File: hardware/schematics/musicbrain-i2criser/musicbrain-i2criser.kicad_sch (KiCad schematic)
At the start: 2 parts, among them J1 BUS, J2 NAAR FRONT

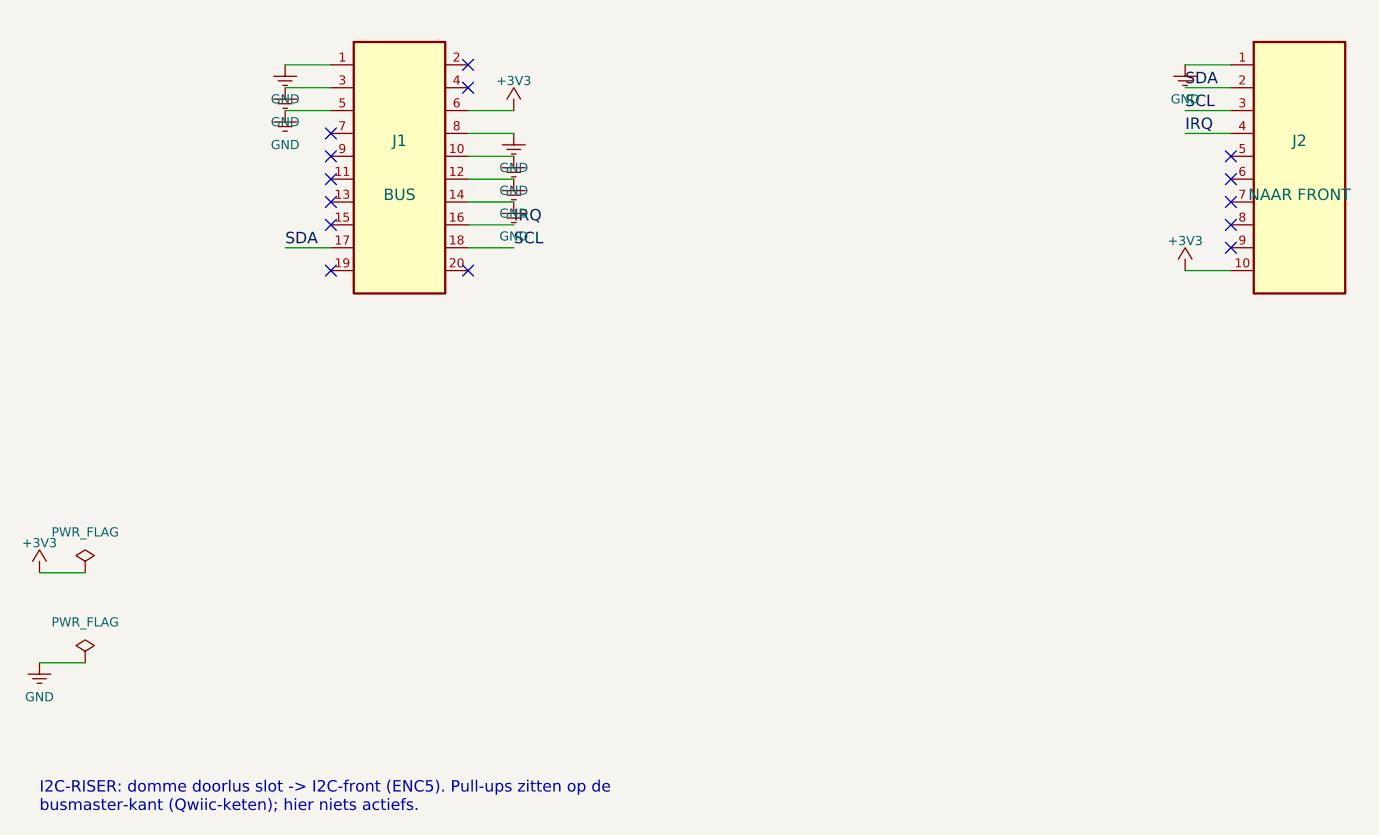
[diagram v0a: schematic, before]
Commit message: Gen 2 stap 2+3a: bus.py + i2criser rev 2.0 (2x12, H=50) DRC 0/0
bus.py = één bron van waarheid voor bus-generatie 2 (spiegel van
spi-bus-spec v2.0): H=50, kaartbreedte 80, slotsteek 20,32, de 24-pins
SLOT-map, de 2x12-footprints en de front-standaard. Generators tikken de
pinout niet meer zelf over.

i2criser rev 2.0 = eerste bord op gen 2 (dom = snelste validatie van de
keten): 40x50 (de 2x12 spant 27,94 -> 28 mm was te smal), J1 2x12, J2 1x10
ongewijzigd. Routing-les: laan-volgorde is kritisch (SDA komt van de kolom
waar SCL naartoe moet -> SDA jogt meteen westwaarts); +3V3 gebruikt de
4 mm vrije strook zuid van J1 i.p.v. de krappe rijcorridor.
ERC 0 / netcheck OK / DRC 0/0.

Co-Authored-By: Claude Fable 5 <noreply@anthropic.com>
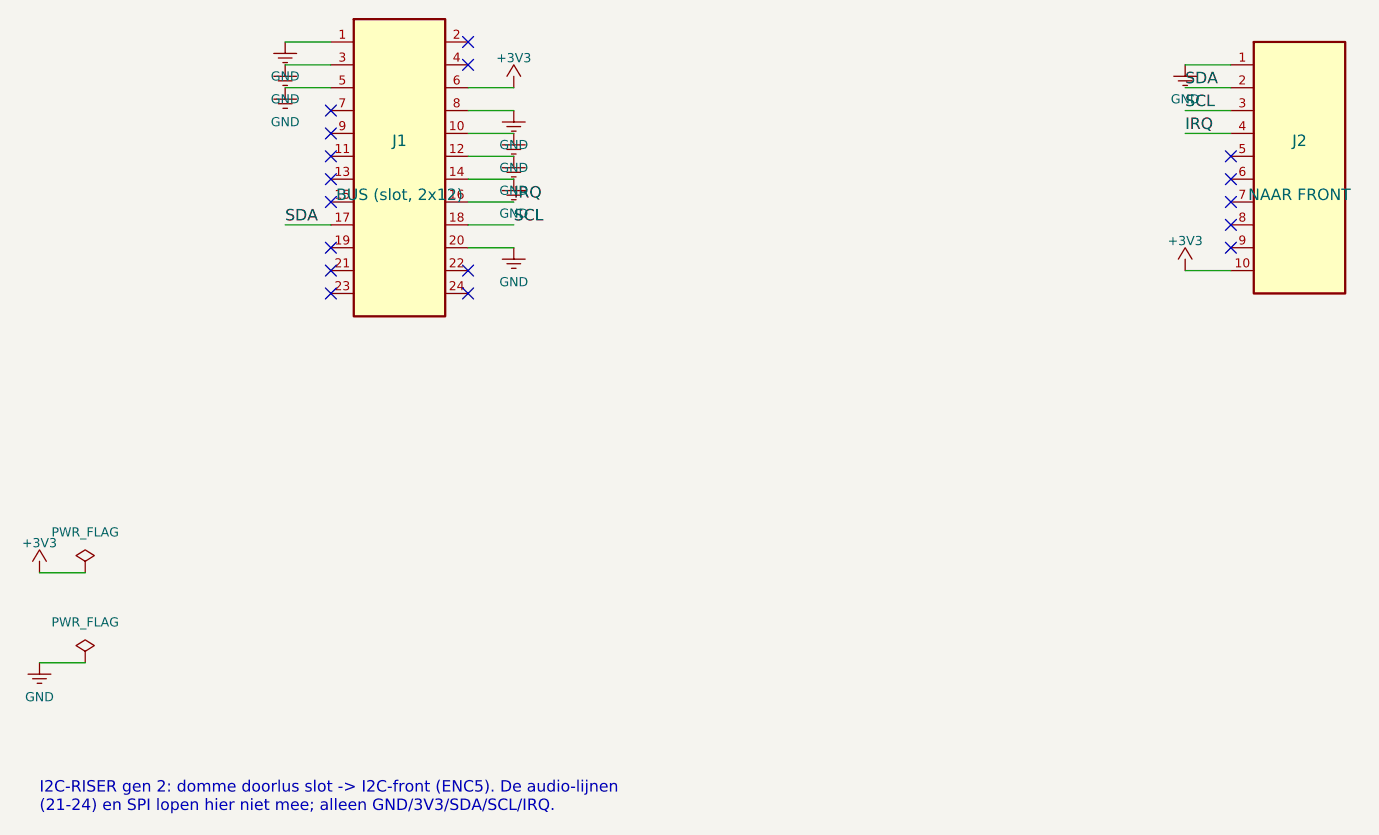
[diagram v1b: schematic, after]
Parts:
- J1: value BUS -> BUS (slot, 2x12); footprint Connector_PinHeader_2.54mm:PinHeader_2x10_P2.54mm_Horizontal -> Connector_PinHeader_2.54mm:PinHeader_2x12_P2.54mm_Horizontal; symbol Custom:Conn_02x10 -> Custom:Conn_02x12
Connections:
- net GND: now also J1.20 (Pin_20)
- no-connect marks 14 -> 17
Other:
- note added: "I2C-RISER gen 2: domme doorlus slot -> I2C-front (ENC5). De audio-lijnen (21-24) en SPI lopen hier niet mee; alleen GND/3V3/SDA/SCL/IRQ."
- note removed: "I2C-RISER: domme doorlus slot -> I2C-front (ENC5). Pull-ups zitten op de busmaster-kant (Qwiic-keten); hier niets actiefs."
